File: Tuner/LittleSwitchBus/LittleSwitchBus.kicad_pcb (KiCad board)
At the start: 2 copper layers, 100 x 100 mm, 99 parts, among them J1 Conn_Coaxial, J10 Conn_Coaxial, J11 Conn_02x05_Odd_Even, J13 Conn_01x01, J14 Conn_01x01, J15 Conn_01x01, J16 Conn_01x01, J2 Conn_Coaxial, J3 Conn_Coaxial, J4 Conn_Coaxial, J5 Conn_Coaxial, J6 Conn_Coaxial, J7 Conn_Coaxial, J8 Conn_Coaxial, J9 Conn_Coaxial, U1 MCP23008, U2 ULN2803A

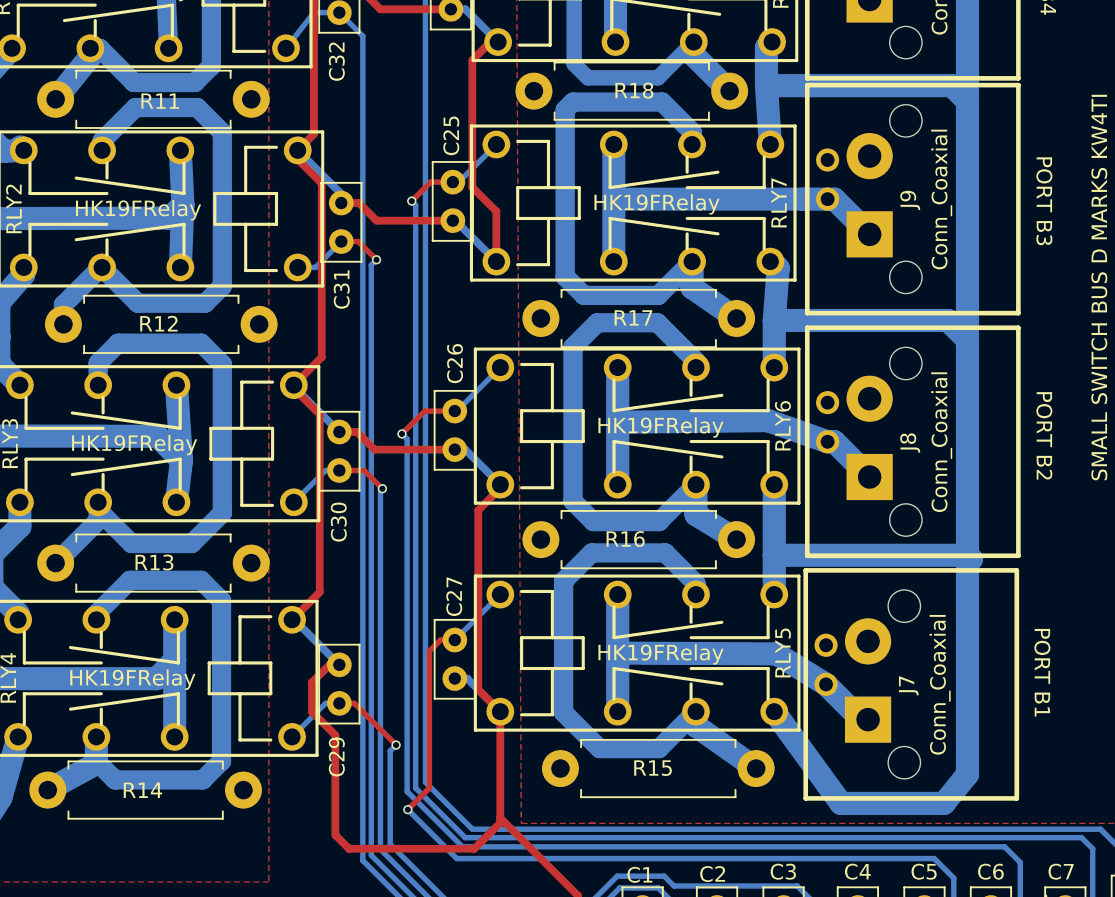
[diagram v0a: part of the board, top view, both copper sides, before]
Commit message: Added OptoisolatedRelay
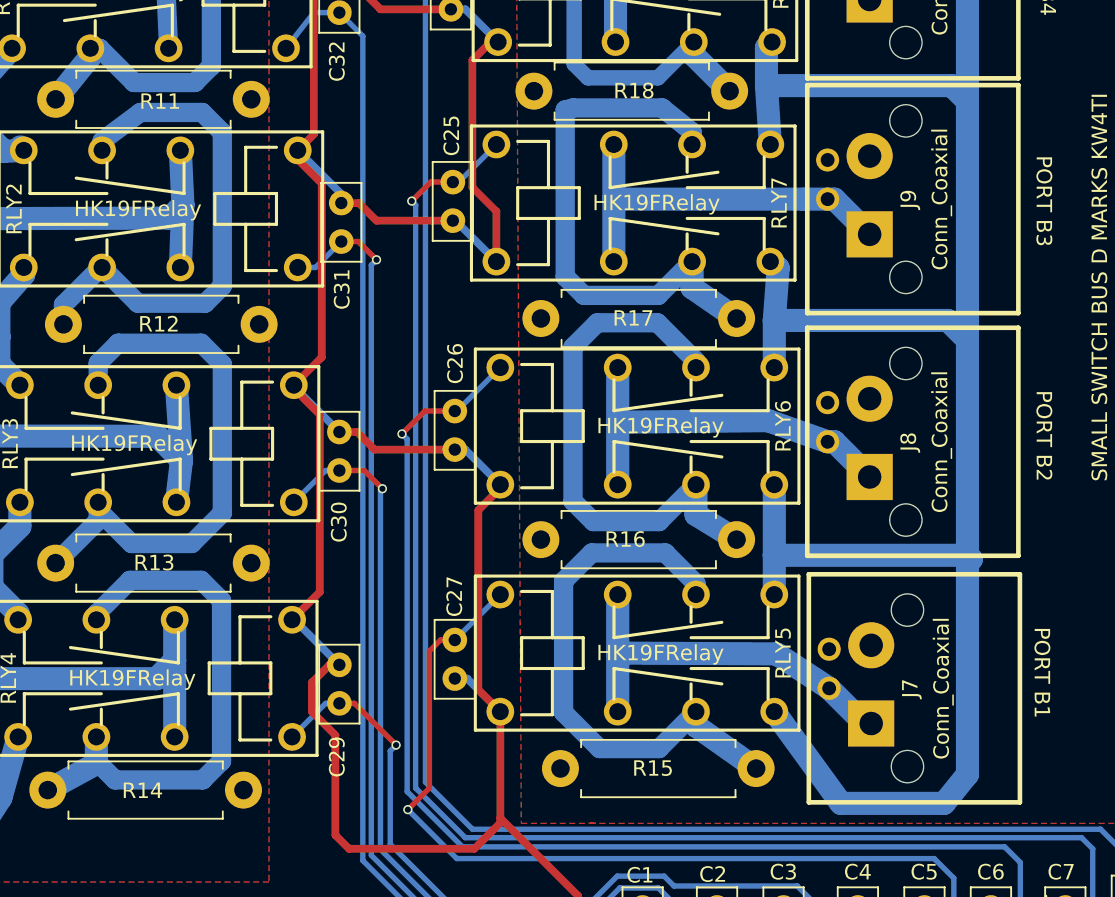
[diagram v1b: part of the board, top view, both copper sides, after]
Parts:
- moved J7 0.33 mm to (140.6, 109.7)
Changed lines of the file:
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@@
   )
   (setup
-    (last_trace_width 1.25)
+    (last_trace_width 0.25)
     (user_trace_width 0.35)
     (user_trace_width 0.5)
@@
   )
   (module tuner:bnc_90_1-1337543-0_pad_combo (layer F.Cu)
-    (at 140.3604 109.474 90)
+    (at 140.5636 109.728 90)
     (descr "BNC connector, Tyco 1-1337543-0")
     (fp_text reference J7 (at 0 -7.112 90) (layer F.SilkS)
@@
   (segment (start 118.618 56.642) (end 120.904 54.356) (width 1.5) (layer B.Cu) (net 7) (status 30))
   (segment (start 114.46 107.442) (end 124.7648 107.4928) (width 1.5) (layer B.Cu) (net 8))
-  (segment (start 124.7648 107.4928) (end 127.9804 109.474) (width 1.5) (layer B.Cu) (net 8) (status 20))
-  (segment (start 130.7084 111.76) (end 130.2664 111.76) (width 1.5) (layer B.Cu) (net 8) (status 30))
-  (segment (start 130.2664 111.76) (end 127.9804 109.474) (width 1.5) (layer B.Cu) (net 8) (status 30))
+  (segment (start 124.7648 107.4928) (end 128.1836 109.728) (width 1.5) (layer B.Cu) (net 8) (status 20))
+  (segment (start 130.4696 112.014) (end 128.1836 109.728) (width 1.5) (layer B.Cu) (net 8) (status 30))
   (segment (start 114.46 103.642) (end 114.46 107.442) (width 1.5) (layer B.Cu) (net 8))
   (segment (start 114.46 107.442) (end 114.46 111.242) (width 1.5) (layer B.Cu) (net 8))
+  (segment (start 130.9116 112.014) (end 130.4696 112.014) (width 1.5) (layer B.Cu) (net 8) (status 30))
   (segment (start 114.31776 64.008) (end 129.794 64.008) (width 1.5) (layer B.Cu) (net 9))
   (segment (start 129.794 64.008) (end 130.81 65.024) (width 1.5) (layer B.Cu) (net 9))
@@
   (segment (start 80.231 68.189) (end 80.231 68.7146) (width 1.5) (layer B.Cu) (net 58) (status 30))
   (segment (start 80.231 68.7146) (end 77.978 71.501) (width 1.5) (layer B.Cu) (net 58) (status 10))
-  (segment (start 80.993 74.201) (end 83.1596 72.0344) (width 1.25) (layer B.Cu) (net 59))
-  (segment (start 83.1596 72.0344) (end 87.1728 72.0344) (width 1.25) (layer B.Cu) (net 59))
-  (segment (start 87.1728 72.0344) (end 88.7984 73.66) (width 1.25) (layer B.Cu) (net 59))
+  (segment (start 80.993 74.201) (end 83.4771 72.3519) (width 1.25) (layer B.Cu) (net 59))
+  (segment (start 83.4771 72.3519) (end 87.4903 72.3519) (width 1.25) (layer B.Cu) (net 59))
+  (segment (start 87.4903 72.3519) (end 88.7984 73.66) (width 1.25) (layer B.Cu) (net 59))
   (segment (start 88.7984 73.66) (end 88.7984 83.6168) (width 1.25) (layer B.Cu) (net 59))
   (segment (start 88.7984 83.6168) (end 87.6808 84.7344) (width 1.25) (layer B.Cu) (net 59))
@@
   (segment (start 119.54 88.91) (end 119.54 88.806) (width 1.5) (layer B.Cu) (net 63))
   (segment (start 119.286 74.432) (end 119.286 73.6168) (width 1.25) (layer B.Cu) (net 64))
-  (segment (start 119.286 73.6168) (end 117.348 71.6788) (width 1.25) (layer B.Cu) (net 64))
+  (segment (start 119.286 73.6168) (end 117.348 72.0598) (width 1.25) (layer B.Cu) (net 64))
   (segment (start 117.0916 84.2264) (end 119.286 82.032) (width 1.25) (layer B.Cu) (net 64))
   (segment (start 112.268 84.2264) (end 117.0916 84.2264) (width 1.25) (layer B.Cu) (net 64))
   (segment (start 111.0488 83.0072) (end 112.268 84.2264) (width 1.25) (layer B.Cu) (net 64))
   (segment (start 111.0488 72.1868) (end 111.0488 83.0072) (width 1.25) (layer B.Cu) (net 64))
-  (segment (start 111.5568 71.6788) (end 111.0488 72.1868) (width 1.25) (layer B.Cu) (net 64))
-  (segment (start 117.348 71.6788) (end 111.5568 71.6788) (width 1.25) (layer B.Cu) (net 64))
+  (segment (start 111.5568 72.0598) (end 111.0488 72.1868) (width 1.25) (layer B.Cu) (net 64))
+  (segment (start 117.348 72.0598) (end 111.5568 72.0598) (width 1.25) (layer B.Cu) (net 64))
   (segment (start 119.286 82.032) (end 119.286 83.726) (width 1.5) (layer B.Cu) (net 64))
   (segment (start 119.286 83.726) (end 122.174 85.725) (width 1.5) (layer B.Cu) (net 64) (status 20))
   (segment (start 119.286 74.432) (end 119.136 74.432) (width 1.5) (layer B.Cu) (net 64))
-  (segment (start 119.39776 60.1826) (end 117.602 60.198) (width 1) (layer B.Cu) (net 65) (status 400000))
+  (segment (start 119.39776 60.1826) (end 117.602 60.198) (width 1) (layer B.Cu) (net 65))
   (segment (start 117.07636 70.104) (end 119.39776 67.7826) (width 1) (layer B.Cu) (net 65))
   (segment (start 112.522 70.104) (end 117.07636 70.104) (width 1) (layer B.Cu) (net 65))

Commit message: Added some fixes to tuner code
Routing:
- net Net-(J6-Pad1): track 163.3 -> 162.3 mm
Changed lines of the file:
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@@
   (segment (start 120.904 54.356) (end 120.904 56.60884) (width 1.5) (layer B.Cu) (net 7) (status 10))
   (segment (start 120.904 56.60884) (end 124.47776 60.1826) (width 1.5) (layer B.Cu) (net 7))
-  (segment (start 124.112 70.612) (end 136.144 70.612) (width 1.5) (layer B.Cu) (net 7))
-  (segment (start 136.144 70.612) (end 137.16 71.628) (width 1.5) (layer B.Cu) (net 7))
-  (segment (start 124.366 74.432) (end 124.112 70.612) (width 1.5) (layer B.Cu) (net 7) (status 10))
-  (segment (start 124.112 70.612) (end 124.112 68.14836) (width 1.5) (layer B.Cu) (net 7))
+  (segment (start 124.874 70.612) (end 136.906 70.612) (width 1.5) (layer B.Cu) (net 7))
+  (segment (start 136.906 70.612) (end 137.16 71.628) (width 1.5) (layer B.Cu) (net 7))
+  (segment (start 124.366 74.432) (end 124.874 70.612) (width 1.5) (layer B.Cu) (net 7) (status 10))
+  (segment (start 124.874 70.612) (end 124.112 68.14836) (width 1.5) (layer B.Cu) (net 7))
   (segment (start 124.112 68.14836) (end 124.47776 67.7826) (width 1.5) (layer B.Cu) (net 7))
-  (segment (start 124.62 85.852) (end 135.89 85.852) (width 1.5) (layer B.Cu) (net 7))
-  (segment (start 135.89 85.852) (end 137.16 87.122) (width 1.5) (layer B.Cu) (net 7))
-  (segment (start 124.62 88.91) (end 124.62 85.852) (width 1.5) (layer B.Cu) (net 7))
-  (segment (start 124.62 85.852) (end 124.874 82.456) (width 1.5) (layer B.Cu) (net 7) (status 20))
+  (segment (start 125.382 85.852) (end 136.652 85.852) (width 1.5) (layer B.Cu) (net 7))
+  (segment (start 136.652 85.852) (end 137.16 87.122) (width 1.5) (layer B.Cu) (net 7))
+  (segment (start 124.62 88.91) (end 125.382 85.852) (width 1.5) (layer B.Cu) (net 7))
+  (segment (start 125.382 85.852) (end 124.874 82.456) (width 1.5) (layer B.Cu) (net 7) (status 20))
   (segment (start 124.874 82.456) (end 124.45 82.032) (width 1.5) (layer B.Cu) (net 7) (status 30))
   (segment (start 124.45 82.032) (end 124.366 82.032) (width 1.5) (layer B.Cu) (net 7) (status 30))
-  (segment (start 124.62 101.092) (end 136.906 101.092) (width 1.5) (layer B.Cu) (net 7))
+  (segment (start 125.255 101.092) (end 136.906 101.092) (width 1.5) (layer B.Cu) (net 7))
   (segment (start 136.906 101.092) (end 137.16 101.346) (width 1.5) (layer B.Cu) (net 7))
-  (segment (start 124.62 103.642) (end 124.62 101.092) (width 1.5) (layer B.Cu) (net 7))
-  (segment (start 124.62 101.092) (end 124.62 96.51) (width 1.5) (layer B.Cu) (net 7))
+  (segment (start 124.62 103.642) (end 125.255 101.092) (width 1.5) (layer B.Cu) (net 7))
+  (segment (start 125.255 101.092) (end 124.62 96.51) (width 1.5) (layer B.Cu) (net 7))
   (segment (start 137.16 101.346) (end 137.414 101.346) (width 1.5) (layer B.Cu) (net 7))
   (segment (start 137.414 101.346) (end 137.16 101.346) (width 1.5) (layer B.Cu) (net 7))

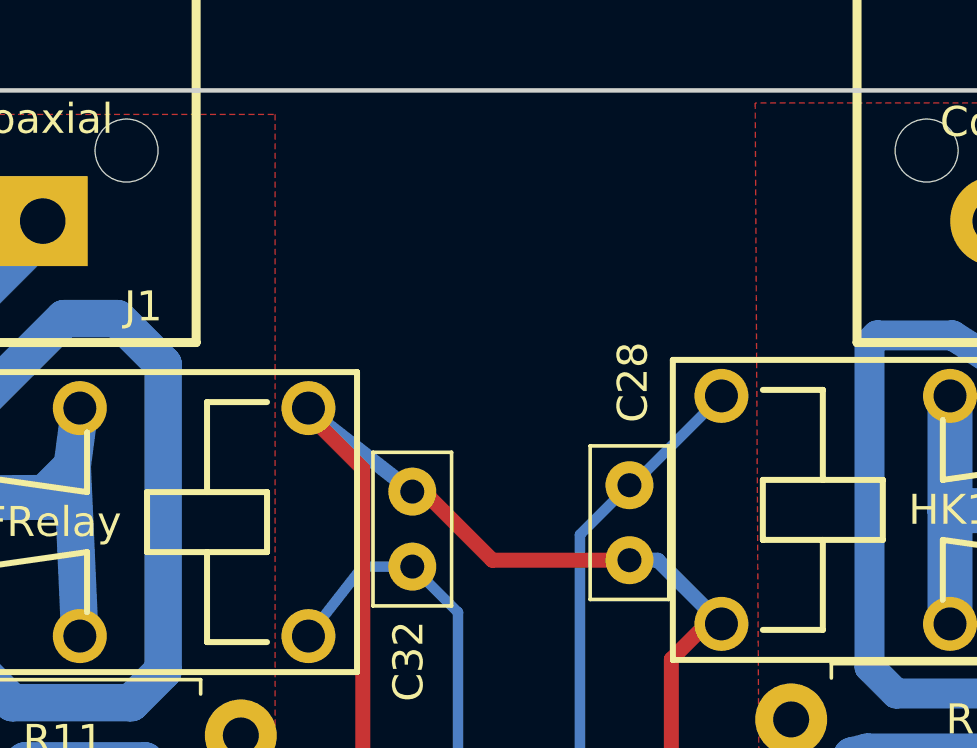
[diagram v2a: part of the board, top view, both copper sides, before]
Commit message: Added extra capacitors between relay power and ground posts
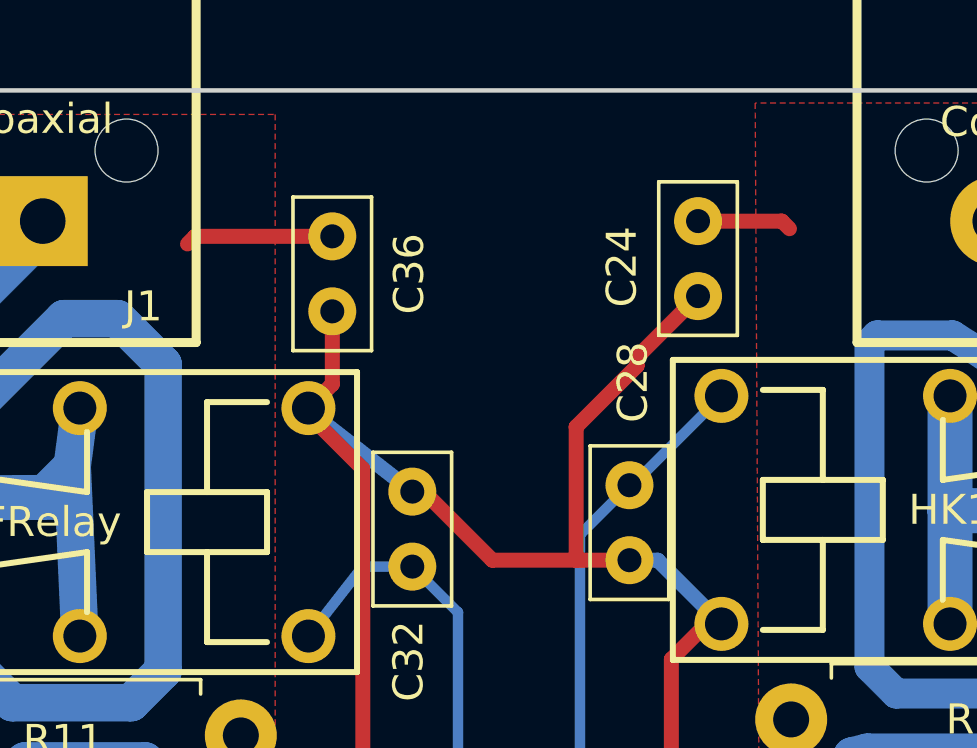
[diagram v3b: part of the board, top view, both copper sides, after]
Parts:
- added C24: 10 nF, Capacitors_THT:C_Disc_D5.0mm_W2.5mm_P2.50mm, F.Cu at (105.9, 54.4)
- added C36: 10 nF, Capacitors_THT:C_Disc_D5.0mm_W2.5mm_P2.50mm, F.Cu at (93.7, 54.9)
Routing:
- net RLYPWR: track 262.1 -> 276.2 mm
- net RFGND: track 2.72 -> 7.65 mm
- net RFGND2: track 0.00 -> 3.15 mm
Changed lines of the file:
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@@
 (kicad_pcb (version 4) (host pcbnew 4.0.7)
   (general
-    (links 239)
+    (links 243)
     (no_connects 0)
     (area 44.281218 44.254 151.75012 153.921938)
     (thickness 1.6)
     (drawings 27)
-    (tracks 884)
+    (tracks 895)
     (zones 0)
-    (modules 99)
+    (modules 101)
     (nets 66)
   )
@@
   )
   (setup
-    (last_trace_width 0.25)
+    (last_trace_width 0.5)
     (user_trace_width 0.35)
     (user_trace_width 0.5)
@@
     )
   )
+  (module Capacitors_THT:C_Disc_D5.0mm_W2.5mm_P2.50mm (layer F.Cu)
+    (at 105.918 54.356 270)
+    (descr "C, Disc series, Radial, pin pitch=2.50mm, , diameter*width=5*2.5mm^2, Capacitor, http://cdn-reichelt.de/documents/datenblatt/B300/DS_KERKO_TC.pdf")
+    (tags "C Disc series Radial pin pitch 2.50mm  diameter 5mm width 2.5mm Capacitor")
+    (fp_text reference C24 (at 1.524 2.54 270) (layer F.SilkS)
+      (effects (font (size 1 1) (thickness 0.15)))
+    )
+    (fp_text value "10 nF" (at 1.25 2.56 270) (layer F.Fab)
+      (effects (font (size 1 1) (thickness 0.15)))
+    )
+    (fp_line (start -1.25 -1.25) (end -1.25 1.25) (layer F.Fab) (width 0.1))
+    (fp_line (start -1.25 1.25) (end 3.75 1.25) (layer F.Fab) (width 0.1))
+    (fp_line (start 3.75 1.25) (end 3.75 -1.25) (layer F.Fab) (width 0.1))
+    (fp_line (start 3.75 -1.25) (end -1.25 -1.25) (layer F.Fab) (width 0.1))
+    (fp_line (start -1.31 -1.31) (end 3.81 -1.31) (layer F.SilkS) (width 0.12))
+    (fp_line (start -1.31 1.31) (end 3.81 1.31) (layer F.SilkS) (width 0.12))
+    (fp_line (start -1.31 -1.31) (end -1.31 1.31) (layer F.SilkS) (width 0.12))
+    (fp_line (start 3.81 -1.31) (end 3.81 1.31) (layer F.SilkS) (width 0.12))
+    (fp_line (start -1.6 -1.6) (end -1.6 1.6) (layer F.CrtYd) (width 0.05))
+    (fp_line (start -1.6 1.6) (end 4.1 1.6) (layer F.CrtYd) (width 0.05))
+    (fp_line (start 4.1 1.6) (end 4.1 -1.6) (layer F.CrtYd) (width 0.05))
+    (fp_line (start 4.1 -1.6) (end -1.6 -1.6) (layer F.CrtYd) (width 0.05))
+    (fp_text user %R (at 1.25 0 270) (layer F.Fab)
+      (effects (font (size 1 1) (thickness 0.15)))
+    )
+    (pad 1 thru_hole circle (at 0 0 270) (size 1.6 1.6) (drill 0.8) (layers *.Cu *.Mask)
+      (net 56 RFGND2))
+    (pad 2 thru_hole circle (at 2.5 0 270) (size 1.6 1.6) (drill 0.8) (layers *.Cu *.Mask)
+      (net 32 RLYPWR))
+    (model ${KISYS3DMOD}/Capacitors_THT.3dshapes/C_Disc_D5.0mm_W2.5mm_P2.50mm.wrl
+      (at (xyz 0 0 0))
+      (scale (xyz 1 1 1))
+      (rotate (xyz 0 0 0))
+    )
+  )
+  (module Capacitors_THT:C_Disc_D5.0mm_W2.5mm_P2.50mm (layer F.Cu)
+    (at 93.726 54.864 270)
+    (descr "C, Disc series, Radial, pin pitch=2.50mm, , diameter*width=5*2.5mm^2, Capacitor, http://cdn-reichelt.de/documents/datenblatt/B300/DS_KERKO_TC.pdf")
+    (tags "C Disc series Radial pin pitch 2.50mm  diameter 5mm width 2.5mm Capacitor")
+    (fp_text reference C36 (at 1.25 -2.56 270) (layer F.SilkS)
+      (effects (font (size 1 1) (thickness 0.15)))
+    )
+    (fp_text value "10 nF" (at 1.25 2.56 270) (layer F.Fab)
+      (effects (font (size 1 1) (thickness 0.15)))
+    )
+    (fp_line (start -1.25 -1.25) (end -1.25 1.25) (layer F.Fab) (width 0.1))
+    (fp_line (start -1.25 1.25) (end 3.75 1.25) (layer F.Fab) (width 0.1))
+    (fp_line (start 3.75 1.25) (end 3.75 -1.25) (layer F.Fab) (width 0.1))
+    (fp_line (start 3.75 -1.25) (end -1.25 -1.25) (layer F.Fab) (width 0.1))
+    (fp_line (start -1.31 -1.31) (end 3.81 -1.31) (layer F.SilkS) (width 0.12))
+    (fp_line (start -1.31 1.31) (end 3.81 1.31) (layer F.SilkS) (width 0.12))
+    (fp_line (start -1.31 -1.31) (end -1.31 1.31) (layer F.SilkS) (width 0.12))
+    (fp_line (start 3.81 -1.31) (end 3.81 1.31) (layer F.SilkS) (width 0.12))
+    (fp_line (start -1.6 -1.6) (end -1.6 1.6) (layer F.CrtYd) (width 0.05))
+    (fp_line (start -1.6 1.6) (end 4.1 1.6) (layer F.CrtYd) (width 0.05))
+    (fp_line (start 4.1 1.6) (end 4.1 -1.6) (layer F.CrtYd) (width 0.05))
+    (fp_line (start 4.1 -1.6) (end -1.6 -1.6) (layer F.CrtYd) (width 0.05))
+    (fp_text user %R (at 1.25 0 270) (layer F.Fab)
+      (effects (font (size 1 1) (thickness 0.15)))
+    )
+    (pad 1 thru_hole circle (at 0 0 270) (size 1.6 1.6) (drill 0.8) (layers *.Cu *.Mask)
+      (net 1 RFGND))
+    (pad 2 thru_hole circle (at 2.5 0 270) (size 1.6 1.6) (drill 0.8) (layers *.Cu *.Mask)
+      (net 32 RLYPWR))
+    (model ${KISYS3DMOD}/Capacitors_THT.3dshapes/C_Disc_D5.0mm_W2.5mm_P2.50mm.wrl
+      (at (xyz 0 0 0))
+      (scale (xyz 1 1 1))
+      (rotate (xyz 0 0 0))
+    )
+  )
   (gr_text "PORT B1" (at 141.986 108.712 270) (layer F.SilkS)
     (effects (font (size 1 1) (thickness 0.15)))
@@
   (gr_line (start 150 150) (end 50 150) (angle 90) (layer Edge.Cuts) (width 0.15))
   (gr_line (start 50 50) (end 150 50) (angle 90) (layer Edge.Cuts) (width 0.15))
+  (segment (start 93.726 54.864) (end 89.154 54.864) (width 0.5) (layer F.Cu) (net 1) (status 400000))
+  (segment (start 89.154 54.864) (end 88.9 55.118) (width 0.5) (layer F.Cu) (net 1))
   (segment (start 53.803 52.197) (end 53 53) (width 1) (layer F.Cu) (net 1) (status 30))
   (segment (start 53 53) (end 53 53.3625) (width 0.5) (layer F.Cu) (net 1) (status 30))
@@
   (segment (start 101.473 148.209) (end 102.108 148.209) (width 0.35) (layer F.Cu) (net 31) (status 30))
   (segment (start 123.4821 148.1709) (end 123.4821 147.7899) (width 0.35) (layer F.Cu) (net 31) (status 30))
+  (segment (start 101.854 65.659) (end 101.854 61.214) (width 0.5) (layer F.Cu) (net 32))
+  (segment (start 103.886 58.888) (end 105.918 56.856) (width 0.5) (layer F.Cu) (net 32) (status 800000))
+  (segment (start 103.886 59.182) (end 103.886 58.888) (width 0.5) (layer F.Cu) (net 32))
+  (segment (start 101.854 61.214) (end 103.886 59.182) (width 0.5) (layer F.Cu) (net 32))
+  (segment (start 93.726 57.364) (end 93.726 59.794) (width 0.5) (layer F.Cu) (net 32) (status 400000))
+  (segment (start 93.726 59.794) (end 92.931 60.589) (width 0.5) (layer F.Cu) (net 32) (status 800000))
   (segment (start 116.078 141.859) (end 115.062 141.859) (width 0.5) (layer F.Cu) (net 32))
   (segment (start 111.887 123.19) (end 106.84 118.143) (width 0.5) (layer F.Cu) (net 32))
@@
   (segment (start 96.393 63.373) (end 96.774 63.373) (width 0.5) (layer F.Cu) (net 32))
   (segment (start 96.774 63.373) (end 99.06 65.659) (width 0.5) (layer F.Cu) (net 32))
-  (segment (start 99.06 65.659) (end 103.632 65.659) (width 0.5) (layer F.Cu) (net 32))
+  (segment (start 99.06 65.659) (end 101.854 65.659) (width 0.5) (layer F.Cu) (net 32))
+  (segment (start 101.854 65.659) (end 103.632 65.659) (width 0.5) (layer F.Cu) (net 32))
   (segment (start 96.52 78.232) (end 97.663 78.232) (width 0.5) (layer F.Cu) (net 32))
   (segment (start 98.806 79.375) (end 103.759 79.375) (width 0.5) (layer F.Cu) (net 32))
@@
   (segment (start 128.524 93.726) (end 130.81 96.012) (width 1.5) (layer B.Cu) (net 55))
   (segment (start 114.46 88.91) (end 114.46 92.456) (width 1.5) (layer B.Cu) (net 55))
+  (segment (start 105.918 54.356) (end 108.712 54.356) (width 0.5) (layer F.Cu) (net 56) (status 400000))
+  (segment (start 108.712 54.356) (end 108.966 54.61) (width 0.5) (layer F.Cu) (net 56))
   (segment (start 128.082 77.978) (end 128.524 77.978) (width 1.5) (layer B.Cu) (net 57))
   (segment (start 128.524 77.978) (end 130.81 80.264) (width 1.5) (layer B.Cu) (net 57))
